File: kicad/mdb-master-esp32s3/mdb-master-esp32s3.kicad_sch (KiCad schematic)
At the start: 36 parts, among them J2 MDB_Connector, J3 Conn_02x09_Odd_Even, P1 USB_C_Plug_USB2.0, SW1 SW_Push, U1 ESP32-S3, U2 W25Q32JVSS, U4 LM317_SOT-223, U5 PC817, U6 PC817, Y1 Crystal

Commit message: Refacting
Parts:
- removed C10: C_Polarized, Capacitor_Tantalum_SMD:CP_EIA-3216-18_Kemet-A, symbol Device:C_Polarized
- removed C7: C, Capacitor_SMD:C_0603_1608Metric, symbol Device:C
- removed D1: D, Diode_SMD:D_SOD-123, symbol Device:D
- removed D3, D4: LED, LED_SMD:LED_0603_1608Metric, symbol Device:LED
- removed D5: D_Zener, Diode_SMD:D_MiniMELF, symbol Device:D_Zener
- removed J3: Conn_02x09_Odd_Even, Connector_PinHeader_2.54mm:PinHeader_2x09_P2.54mm_Vertical, symbol Connector_Generic:Conn_02x09_Odd_Even
- removed R13, R14: R, Resistor_SMD:R_0805_2012Metric, symbol Device:R
- removed U2: W25Q32JVSS, Package_SON:WSON-8-1EP_8x6mm_P1.27mm_EP3.4x4.3mm, symbol Memory_Flash:W25Q32JVSS
- removed U4: LM317_SOT-223, Package_TO_SOT_SMD:SOT-223-3_TabPin2, symbol Regulator_Linear:LM317_SOT-223
- removed U5, U6: PC817, Package_DIP:DIP-4_W7.62mm, symbol Isolator:PC817
- added BZ1: Buzzer, Buzzer_Beeper:Buzzer_12x9.5RM7.6, symbol Device:Buzzer
- added C2: C, Capacitor_SMD:C_0603_1608Metric, symbol Device:C
- added C7: C_Polarized, Capacitor_Tantalum_SMD:CP_EIA-3216-18_Kemet-A, symbol Device:C_Polarized
- added D1, D2: LED, LED_SMD:LED_0603_1608Metric, symbol Device:LED
- added D3: D, Diode_SMD:D_SOD-123, symbol Device:D
- added J1: Conn_02x09_Odd_Even, Connector_PinHeader_2.54mm:PinHeader_2x09_P2.54mm_Vertical, symbol Connector_Generic:Conn_02x09_Odd_Even
- added J3: Barrel_Jack, Connector_BarrelJack:BarrelJack_Horizontal, symbol Connector:Barrel_Jack
- added Q1: BC807, Package_TO_SOT_SMD:SOT-23, symbol Transistor_BJT:BC807
- added R16, R17, R7: R, Resistor_SMD:R_0603_1608Metric, symbol Device:R
- added SW2: Boot, Button_Switch_SMD:SW_Tactile_SPST_NO_Straight_CK_PTS636Sx25SMTRLFS, symbol Switch:SW_Push
- added U2: LM317_SOT-223, Package_TO_SOT_SMD:SOT-223-3_TabPin2, symbol Regulator_Linear:LM317_SOT-223
- R11, R15: footprint Resistor_SMD:R_0805_2012Metric -> Resistor_SMD:R_0603_1608Metric
- R8: value R -> 240
- SW1: value SW_Push -> Reset
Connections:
- net mdb_communications_common is gone; now on net GND: J2.6 (Pin_6)
- net mdb_slave_transmit is gone; now on net io5: U1.10 (GPIO5/ADC1_CH4)
- net +36V: now also D3.1 (K), J3.1, U2.3 (VI)
- net +3V3: now also C3.2, R6.2, R8.1, C2.2, C7.1, D2.2 (A), J1.18 (Pin_18), Q1.2 (E), R17.1, U2.2 (VO); no longer C5.2, R15.2, R3.2
- net GND: now also R2.1, R3.1, R9.2, BZ1.2 (-), C2.1, C7.2, J1.1 (Pin_1), J1.16 (Pin_16), J3.2, R16.2, R7.2, SW2.2; no longer R2.2, R6.2, R8.1, R9.1
- net boot: now also R6.1, SW2.1; no longer R3.1
- net io1: now also J1.7 (Pin_7)
- net io10: now also J1.6 (Pin_6)
- net io11: now also J1.8 (Pin_8)
- net io12: now also J1.10 (Pin_10)
- net io13: now also J1.12 (Pin_12)
- net io14: now also J1.14 (Pin_14)
- net io17: now also J1.15 (Pin_15)
- net io18: now also J1.17 (Pin_17)
- net io2: now also J1.9 (Pin_9)
- net io21: now also D1.2 (A)
- net io6: now also BZ1.1 (+), J1.11 (Pin_11)
- net io7: now also J1.13 (Pin_13)
- net io8: now also J1.2 (Pin_2)
- net io9: now also J1.4 (Pin_4)
- net mdb_master_transmit: now also Q1.3 (C), R16.1
- net u0rxd: now also J1.5 (Pin_5)
- net u0txd: now also J1.3 (Pin_3)
- net at U1.54 (XTAL_P), Y1.1: now also C5.2; no longer C4.2
- net at R8.2: now also R7.1, U2.1 (ADJ)
- net at R11.1: now also P1.A5 (CC)
- net at U1.51 (GPIO45): now also R5.1; no longer R4.1
- net at U1.53 (XTAL_N), Y1.2: now also C4.2; no longer C3.2
- net at U1.52 (GPIO46): now also R4.1; no longer R2.1
- net at P1.A4 (VBUS), P1.A9 (VBUS), P1.B4 (VBUS)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: now also D3.2 (A)
- net at R10.1: now also P1.B5 (VCONN); no longer P1.A5 (CC)
- net at P1.S1 (SHIELD): now also R9.1; no longer R5.1
- net mdb_master_receive renamed io4
- net io4: now also U1.9 (GPIO4/ADC1_CH3), R17.2
- net mdb_slave_receive renamed io5
- net io5: no longer U1.9 (GPIO4/ADC1_CH3)
- net spiclk: no longer names the net of U1.33 (SPICLK/GPIO30)
- net spics0: no longer names the net of U1.32 (SPICS0/GPIO29)
- net spid: no longer names the net of U1.35 (SPID/GPIO32)
- net spihd: no longer names the net of U1.30 (SPIHD/GPIO27)
- net spiq: no longer names the net of U1.34 (SPIQ/GPIO31)
- net spiwp: no longer names the net of U1.31 (SPIWP/GPIO28)
- new net: Q1.1 (B), R15.2
- new net: D2.1 (K), R3.2
- new net: D1.1 (K), R2.2
- no-connect marks 17 -> 23
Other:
- note added: "ESP32-S3FH4R2"
- note removed: "ESP32-S3R8"
- note removed: "W25Q256JVEIQ"

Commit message: Refacting
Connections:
- net io6: no longer J1.11 (Pin_11)
- net vdd_spi: no longer names the net of U1.29 (VDD_SPI)
- no-connect marks 23 -> 25
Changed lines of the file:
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@@
+	)
+	(no_connect
+		(at 60.96 256.54)
 	)
 	(no_connect
@@
 	)
 	(no_connect
+		(at 128.27 138.43)
+	)
+	(no_connect
 		(at 102.87 201.93)
 	)
@@
 	(wire
 		(pts
-			(xy 57.15 256.54) (xy 60.96 256.54)
-		)
-		(stroke
-			(width 0)
-			(type default)
-		)
-	)
-	(wire
-		(pts
 			(xy 97.79 163.83) (xy 97.79 161.29)
 		)
@@
 		(pts
 			(xy 49.53 243.84) (xy 60.96 243.84)
-		)
-		(stroke
-			(width 0)
-			(type default)
-		)
-	)
-	(wire
-		(pts
-			(xy 128.27 132.08) (xy 128.27 138.43)
 		)
 		(stroke
@@
 		)
 	)
-	(label "io6"
-		(at 57.15 256.54 180)
-		(fields_autoplaced yes)
-		(effects
-			(font
-				(size 1.27 1.27)
-			)
-			(justify right bottom)
-		)
-	)
 	(label "io9"
 		(at 77.47 246.38 0)
@@
 		(fields_autoplaced yes)
 		(effects
-			(font
-				(size 1.27 1.27)
-			)
-			(justify left bottom)
-		)
-	)
-	(label "vdd_spi"
-		(at 128.27 132.08 90)
-		(fields_autoplaced yes)
-		(effects

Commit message: refacting
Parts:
- removed J1: Conn_02x09_Odd_Even, Connector_PinHeader_2.54mm:PinHeader_2x09_P2.54mm_Vertical, symbol Connector_Generic:Conn_02x09_Odd_Even
- added J4: Conn_02x08_Odd_Even, Connector_PinHeader_2.54mm:PinHeader_2x08_P2.54mm_Vertical, symbol Connector_Generic:Conn_02x08_Odd_Even
- added TP1, TP2, TP3: TestPoint, TestPoint:TestPoint_Pad_D1.0mm, symbol Connector:TestPoint
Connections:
- net +3V3: now also J4.16 (Pin_16), TP2.1
- net GND: now also J4.1 (Pin_1), TP3.1
- net io1: now also J4.7 (Pin_7)
- net io10: now also J4.6 (Pin_6)
- net io11: now also J4.8 (Pin_8)
- net io12: now also J4.10 (Pin_10)
- net io13: now also J4.12 (Pin_12)
- net io14: now also J4.14 (Pin_14)
- net io17: now also J4.13 (Pin_13)
- net io18: now also J4.15 (Pin_15)
- net io2: now also J4.9 (Pin_9)
- net io7: now also J4.11 (Pin_11)
- net io8: now also J4.2 (Pin_2)
- net io9: now also J4.4 (Pin_4)
- net u0rxd: now also J4.5 (Pin_5)
- net u0txd: now also J4.3 (Pin_3)
- net +36V renamed vin
- net vin: now also TP1.1
- no-connect marks 25 -> 24

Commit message: Refacting
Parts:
- removed J4: Conn_02x08_Odd_Even, Connector_PinHeader_2.54mm:PinHeader_2x08_P2.54mm_Vertical, symbol Connector_Generic:Conn_02x08_Odd_Even
- added J5: Conn_02x10_Odd_Even, Connector_PinHeader_2.54mm:PinHeader_2x10_P2.54mm_Vertical, symbol Connector_Generic:Conn_02x10_Odd_Even
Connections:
- net +3V3: now also J5.18 (Pin_18)
- net GND: now also J5.1 (Pin_1), J5.3 (Pin_3)
- net io1: now also J5.9 (Pin_9)
- net io10: now also J5.8 (Pin_8)
- net io11: now also J5.10 (Pin_10)
- net io12: now also J5.12 (Pin_12)
- net io13: now also J5.14 (Pin_14)
- net io14: now also J5.16 (Pin_16)
- net io17: now also J5.17 (Pin_17)
- net io18: now also J5.19 (Pin_19)
- net io2: now also J5.11 (Pin_11)
- net io4: now also J5.13 (Pin_13)
- net io5: now also J5.15 (Pin_15)
- net io7: now also J5.2 (Pin_2)
- net io8: now also J5.4 (Pin_4)
- net io9: now also J5.6 (Pin_6)
- net u0rxd: now also J5.7 (Pin_7)
- net u0txd: now also J5.5 (Pin_5)
- net vin: now also J5.20 (Pin_20)

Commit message: Refacting
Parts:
- U1: value ESP32-S3 -> ESP32-S3FH4R2
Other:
- note removed: "ESP32-S3FH4R2"
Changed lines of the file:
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@@
-		)
-	)
-	(text "ESP32-S3FH4R2"
-		(exclude_from_sim no)
-		(at 153.67 138.43 0)
-		(effects
-			(font
-				(size 1.27 1.27)
-			)
-			(justify left bottom)
 		)
 	)
@@
 			)
 		)
-		(property "Value" "ESP32-S3"
+		(property "Value" "ESP32-S3FH4R2"
 			(at 138.0841 222.25 0)
 			(effects

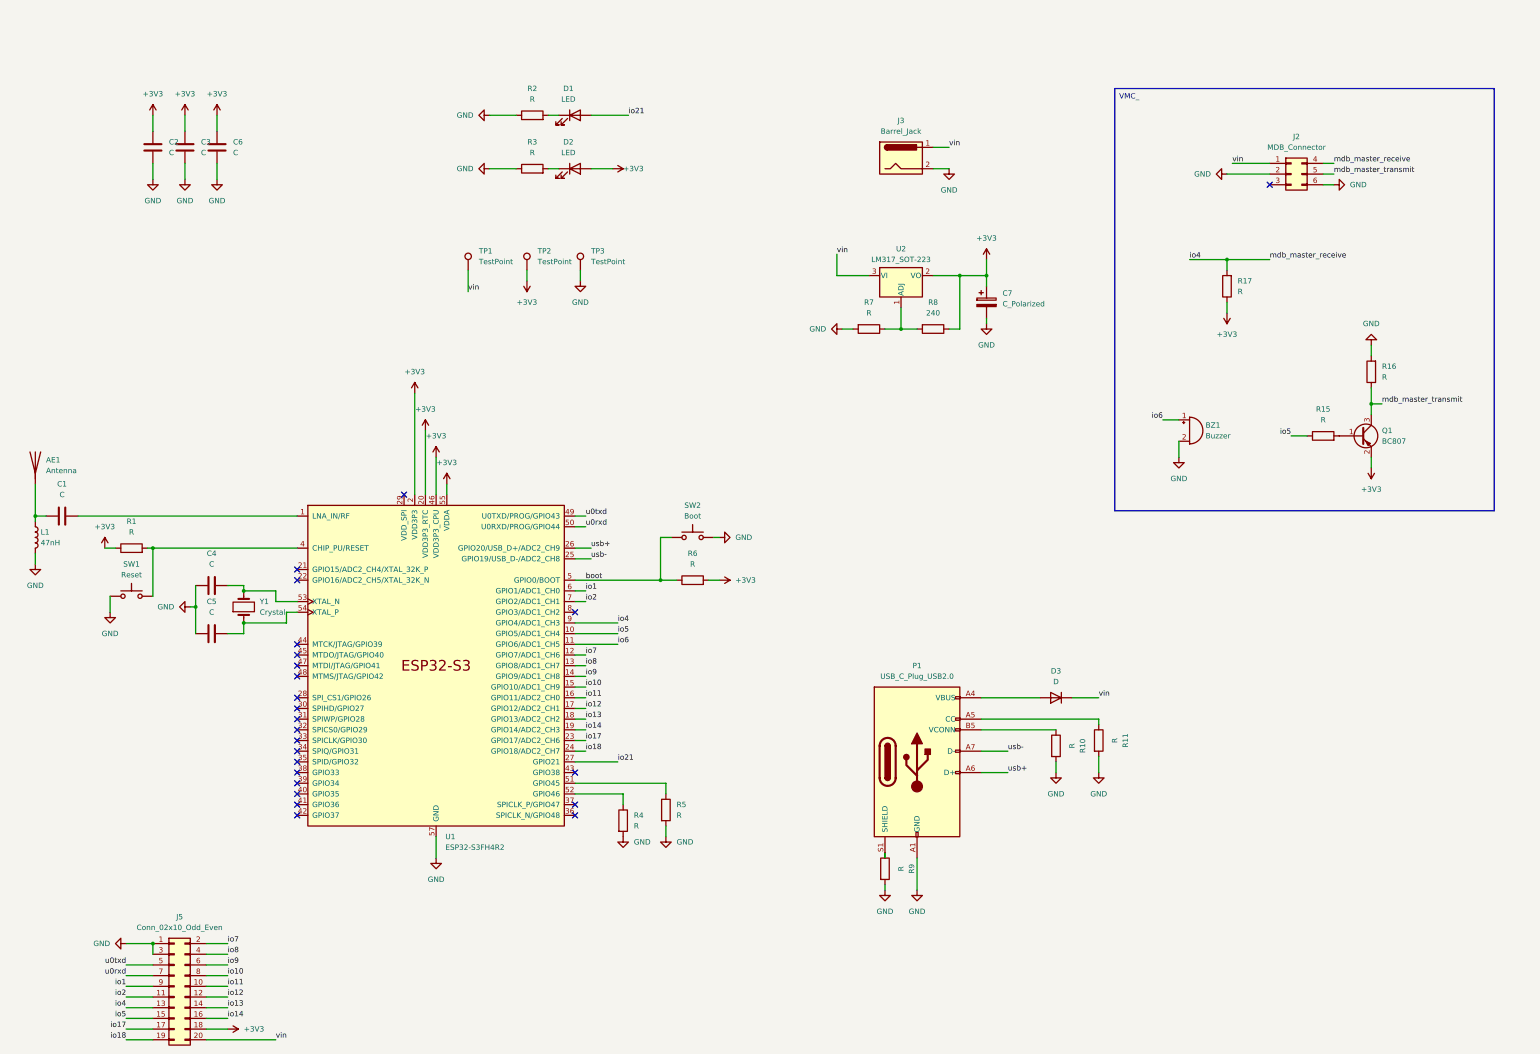
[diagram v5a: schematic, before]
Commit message: Updating POM list
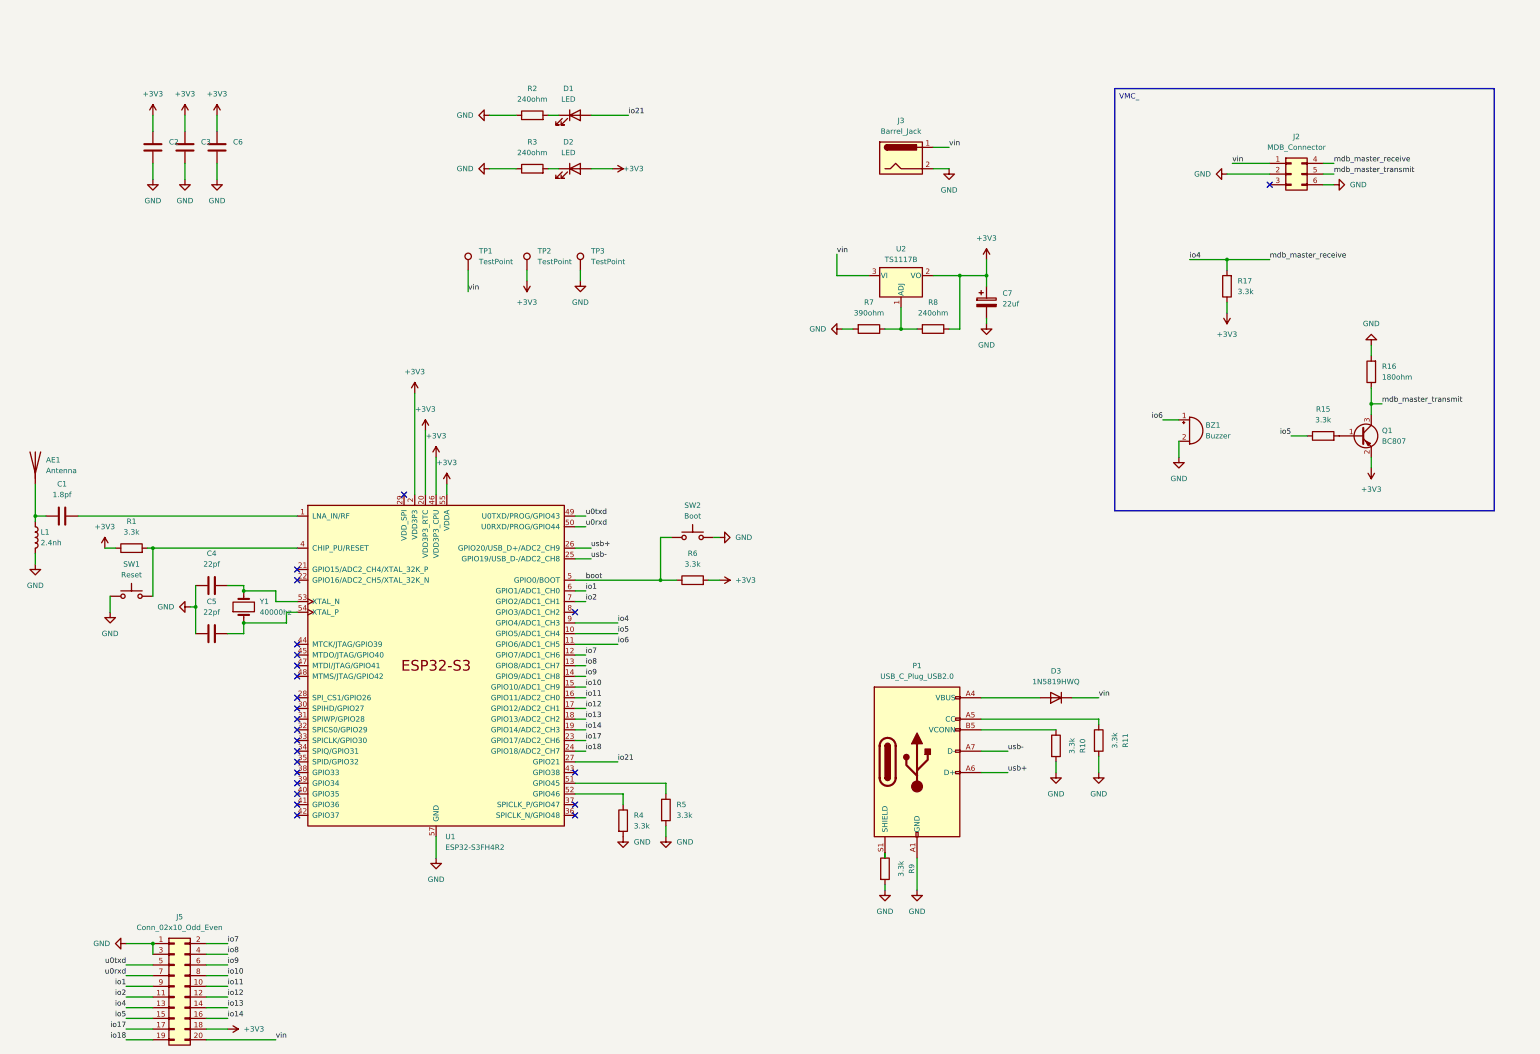
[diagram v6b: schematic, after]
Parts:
- C1: value C -> 1.8pf
- C4, C5: value C -> 22pf
- C7: value C_Polarized -> 22uf
- D3: value D -> 1N5819HWQ
- L1: value 47nH -> 2.4nh
- R1, R10, R11, R15, R17, R4, R5, R6, R9: value R -> 3.3k
- R16: value R -> 180ohm
- R2, R3: value R -> 240ohm
- R7: value R -> 390ohm
- R8: value 240 -> 240ohm
- U2: value LM317_SOT-223 -> TS1117B
- Y1: value Crystal -> 40000hz
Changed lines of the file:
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@@
 			)
 		)
-		(property "Value" "47nH"
+		(property "Value" "2.4nh"
 			(at 41.91 149.86 0)
 			(effects
@@
 			)
 		)
-		(property "Value" "R"
+		(property "Value" "240ohm"
 			(at 158.75 57.15 90)
 			(effects
@@
 			)
 		)
-		(property "Value" "R"
+		(property "Value" "3.3k"
 			(at 193.04 214.63 0)
 			(effects
@@
 				)
 				(justify right)
+				(hide yes)
 			)
 		)
@@
 			)
 		)
-		(property "Value" "R"
+		(property "Value" "3.3k"
 			(at 63.5 147.32 90)
 			(effects
@@
 			)
 		)
-		(property "Value" "C_Polarized"
+		(property "Value" "22uf"
 			(at 270.51 93.0909 0)
 			(effects
@@
 			)
 		)
-		(property "Value" "R"
+		(property "Value" "3.3k"
 			(at 246.38 227.33 90)
 			(effects
@@
 			)
 		)
-		(property "Value" "C"
+		(property "Value" "1.8pf"
 			(at 46.99 138.43 90)
 			(effects
@@
 				)
 				(justify right)
+				(hide yes)
 			)
 		)
@@
 			)
 		)
-		(property "Value" "Crystal"
+		(property "Value" "40000hz"
 			(at 93.98 166.37 90)
 			(effects
@@
 			)
 		)
-		(property "Value" "R"
+		(property "Value" "3.3k"
 			(at 287.02 198.12 90)
 			(effects
@@
 			)
 		)
-		(property "Value" "240"
+		(property "Value" "240ohm"
 			(at 254 95.25 90)
 			(effects
@@
 			)
 		)
-		(property "Value" "R"
+		(property "Value" "3.3k"
 			(at 346.71 120.65 90)
 			(effects
@@
 			)
 		)
-		(property "Value" "R"
+		(property "Value" "3.3k"
 			(at 182.88 217.17 0)
 			(effects
@@
 			)
 		)
-		(property "Value" "R"
+		(property "Value" "240ohm"
 			(at 158.75 44.45 90)
 			(effects
@@
 			)
 		)
-		(property "Value" "R"
+		(property "Value" "3.3k"
 			(at 196.85 154.94 90)
 			(effects
@@
 			)
 		)
-		(property "Value" "R"
+		(property "Value" "390ohm"
 			(at 238.76 95.25 90)
 			(effects
@@
 			)
 		)
-		(property "Value" "R"
+		(property "Value" "3.3k"
 			(at 297.18 196.85 90)
 			(effects
@@
 			)
 		)
-		(property "Value" "R"
+		(property "Value" "3.3k"
 			(at 326.39 90.1699 0)
 			(effects
@@
 			)
 		)
-		(property "Value" "D"
+		(property "Value" "1N5819HWQ"
 			(at 283.21 182.88 0)
 			(effects
@@
 				)
 				(justify right)
+				(hide yes)
 			)
 		)
@@
 			)
 		)
-		(property "Value" "LM317_SOT-223"
+		(property "Value" "TS1117B"
 			(at 246.38 82.55 0)
 			(effects
@@
 			)
 		)
-		(property "Value" "C"
+		(property "Value" "22pf"
 			(at 82.55 154.94 90)
 			(effects
@@
 			)
 		)
-		(property "Value" "C"
+		(property "Value" "22pf"
 			(at 82.55 166.37 90)
 			(effects
@@
 			)
 		)
-		(property "Value" "R"
+		(property "Value" "180ohm"
 			(at 360.68 110.4899 0)
 			(effects

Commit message: Refacting kicad pcb
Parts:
- removed BZ1: Buzzer, Buzzer_Beeper:Buzzer_12x9.5RM7.6, symbol Device:Buzzer
- removed C3: C, Capacitor_SMD:C_0603_1608Metric, symbol Device:C
- removed C7: 22uf, Capacitor_Tantalum_SMD:CP_EIA-3216-18_Kemet-A, symbol Device:C_Polarized
- removed D1: LED, LED_SMD:LED_0603_1608Metric, symbol Device:LED
- removed D3: 1N5819HWQ, Diode_SMD:D_SOD-123, symbol Device:D
- removed J2: MDB_Connector, Connector_Molex:Molex_Mini-Fit_Jr_5566-06A_2x03_P4.20mm_Vertical, symbol Connector_Generic:Conn_02x03_Top_Bottom
- removed J3: Barrel_Jack, Connector_BarrelJack:BarrelJack_Horizontal, symbol Connector:Barrel_Jack
- removed J5: Conn_02x10_Odd_Even, Connector_PinHeader_2.54mm:PinHeader_2x10_P2.54mm_Vertical, symbol Connector_Generic:Conn_02x10_Odd_Even
- removed P1: USB_C_Plug_USB2.0, Connector_USB:USB_C_Receptacle_G-Switch_GT-USB-7010ASV, symbol Connector:USB_C_Plug_USB2.0
- removed R15, R17: 3.3k, Resistor_SMD:R_0603_1608Metric, symbol Device:R
- removed R16: 180ohm, Resistor_SMD:R_0603_1608Metric, symbol Device:R
- removed SW2: Boot, Button_Switch_SMD:SW_Tactile_SPST_NO_Straight_CK_PTS636Sx25SMTRLFS, symbol Switch:SW_Push
- removed TP1, TP3: TestPoint, TestPoint:TestPoint_Pad_D1.0mm, symbol Connector:TestPoint
- removed U2: TS1117B, Package_TO_SOT_SMD:SOT-223-3_TabPin2, symbol Regulator_Linear:LM317_SOT-223
- added C7: 22pf, Capacitor_SMD:C_0603_1608Metric, symbol Device:C
- added D1: 1N5819HWQ, Diode_SMD:D_SOD-123, symbol Device:D
- added D3: LED, LED_SMD:LED_0603_1608Metric, symbol Device:LED
- added J1: MDB_Connector, Connector_Molex:Molex_Mini-Fit_Jr_5566-06A_2x03_P4.20mm_Vertical, symbol Connector_Generic:Conn_02x03_Top_Bottom
- added J2: Barrel_Jack, Connector_BarrelJack:BarrelJack_Horizontal, symbol Connector:Barrel_Jack
- added J3: USB_C_Receptacle_USB2.0_16P, Connector_USB:USB_C_Receptacle_G-Switch_GT-USB-7010ASV, symbol Connector:USB_C_Receptacle_USB2.0_16P
- added J4: Conn_02x11_Odd_Even, Connector_PinHeader_2.54mm:PinHeader_2x11_P2.54mm_Vertical, symbol Connector_Generic:Conn_02x11_Odd_Even
- added U2: AMS1117-3.3, Package_TO_SOT_SMD:SOT-223, symbol Regulator_Linear:AMS1117-3.3
- AE1: footprint RF_Antenna:Texas_SWRA117D_2.4GHz_Right -> RF_Antenna:Texas_SWRA117D_2.4GHz_Left
- C1: value 1.8pf -> C
- C4: value 22pf -> 1.8pf
- C6: value C -> 22pf
- R10, R11: value 3.3k -> 240ohm
- R2: value 240ohm -> 180ohm
- R3, R8: value 240ohm -> 3.3k
- R7: value 390ohm -> 3.3k
- SW1: value Reset -> SW_Push
- U1: value ESP32-S3FH4R2 -> ESP32-S3R8
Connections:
- net +3V3: now also C1.2, C2.1, R11.2, R3.1, R4.2, C7.2, J4.18 (Pin_18), U2.2 (VO); no longer C2.2, C6.2, D2.2 (A), R6.2, R8.1, TP2.1
- net GND: now also C1.1, C2.2, D2.1 (K), L1.1, R2.2, R6.2, R8.2, SW1.2, C7.1, D3.1 (K), J1.2 (Pin_2), J1.6 (Pin_6), J2.2, J3.A1 (GND), J3.A12 (GND), J3.B1 (GND), J3.B12 (GND), J3.S1 (SHIELD), J4.20 (Pin_20), U2.1 (GND); no longer C2.1, C4.1, L1.2, R10.2, R11.2, R2.1, R3.1, R4.2, R5.2, SW1.1
- net boot: now also R4.1, SW1.1, J4.16 (Pin_16); no longer R6.1
- net io1: now also J4.5 (Pin_5)
- net io10: now also J4.6 (Pin_6)
- net io11: now also J4.8 (Pin_8)
- net io12: now also J4.10 (Pin_10)
- net io13: now also J4.12 (Pin_12)
- net io14: now also J4.14 (Pin_14)
- net io17: now also J4.17 (Pin_17)
- net io18: now also J4.19 (Pin_19)
- net io2: now also J4.7 (Pin_7)
- net io21: now also R10.2, J4.21 (Pin_21)
- net io4: now also R1.2, J1.4 (Pin_4), J4.9 (Pin_9)
- net io5: now also R5.1, J4.11 (Pin_11)
- net io6: now also J4.13 (Pin_13)
- net io7: now also J4.15 (Pin_15)
- net io8: now also J4.2 (Pin_2)
- net io9: now also J4.4 (Pin_4)
- net mdb_master_transmit: now also R2.1, J1.5 (Pin_5)
- net u0rxd: now also J4.3 (Pin_3)
- net u0txd: now also J4.1 (Pin_1)
- net usb+: now also J3.A6 (D+), J3.B6 (D+)
- net usb-: now also J3.A7 (D-), J3.B7 (D-)
- net vin: now also D1.1 (K), J1.1 (Pin_1), J2.1, J4.22 (Pin_22), U2.3 (VI)
- net at Q1.1 (B): now also R5.2
- net at R3.2: now also TP2.1, U1.4 (CHIP_PU/RESET); no longer D2.1 (K)
- net at U1.51 (GPIO45): now also R6.1; no longer R5.1
- net at U1.1 (LNA_IN/RF): now also C4.2; no longer C1.2
- net vdd_spi: now reaches U1.29 (VDD_SPI)
- net spihd: now reaches U1.30 (SPIHD/GPIO27)
- net spiwp: now reaches U1.31 (SPIWP/GPIO28)
- net spics0: now reaches U1.32 (SPICS0/GPIO29)
- net spiclk: now reaches U1.33 (SPICLK/GPIO30)
- net spiq: now reaches U1.34 (SPIQ/GPIO31)
- net spid: now reaches U1.35 (SPID/GPIO32)
- net at U1.52 (GPIO46): now also R7.1; no longer R4.1
- net at U1.53 (XTAL_N), Y1.2: now also C5.2; no longer C4.2
- net at U1.54 (XTAL_P), Y1.1: now also C6.2; no longer C5.2
- net at R9.1: now also J3.A5 (CC1)
- net at R10.1: now also D2.2 (A)
- net at R11.1: now also D3.2 (A)
- new net: AE1.1 (A), C4.1, L1.2
- new net: D1.2 (A), J3.A4 (VBUS), J3.A9 (VBUS), J3.B4 (VBUS), J3.B9 (VBUS)
- new net: J3.B5 (CC2), R8.1
- no-connect marks 24 -> 26
